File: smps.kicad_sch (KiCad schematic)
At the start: 36 parts, among them J1 Screw_Terminal_01x02, J4 Screw_Terminal_01x02, U1 LT8640S

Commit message: Cosmetic updates
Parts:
- H1, H2, H3, H4: footprint MountingHole:MountingHole_3.2mm_M3_Pad -> MountingHole:MountingHole_3.2mm_M3
- renumbered TP2 to TP1, TP1 to TP2
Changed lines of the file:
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@@
       (effects (font (size 1.27 1.27)) (justify left))
     )
-    (property "Footprint" "MountingHole:MountingHole_3.2mm_M3_Pad" (id 2) (at 16.51 182.88 0)
+    (property "Footprint" "MountingHole:MountingHole_3.2mm_M3" (id 2) (at 16.51 182.88 0)
       (effects (font (size 1.27 1.27)) hide)
     )
@@
       (effects (font (size 1.27 1.27)) (justify left))
     )
-    (property "Footprint" "MountingHole:MountingHole_3.2mm_M3_Pad" (id 2) (at 16.51 187.96 0)
+    (property "Footprint" "MountingHole:MountingHole_3.2mm_M3" (id 2) (at 16.51 187.96 0)
       (effects (font (size 1.27 1.27)) hide)
     )
@@
   (symbol (lib_id "Connector:TestPoint") (at 142.24 109.22 270) (unit 1)
     (in_bom yes) (on_board yes)
-    (property "Reference" "TP2" (id 0) (at 143.51 111.76 90)
+    (property "Reference" "TP1" (id 0) (at 140.97 111.76 90)
       (effects (font (size 1.27 1.27)) (justify left))
     )
@@
   (symbol (lib_id "Connector:TestPoint") (at 142.24 119.38 270) (unit 1)
     (in_bom yes) (on_board yes)
-    (property "Reference" "TP1" (id 0) (at 143.51 121.92 90)
+    (property "Reference" "TP2" (id 0) (at 140.97 121.92 90)
       (effects (font (size 1.27 1.27)) (justify left))
     )
@@
       (effects (font (size 1.27 1.27)) (justify left))
     )
-    (property "Footprint" "MountingHole:MountingHole_3.2mm_M3_Pad" (id 2) (at 16.51 177.8 0)
+    (property "Footprint" "MountingHole:MountingHole_3.2mm_M3" (id 2) (at 16.51 177.8 0)
       (effects (font (size 1.27 1.27)) hide)
     )
@@
       (effects (font (size 1.27 1.27)) (justify left))
     )
-    (property "Footprint" "MountingHole:MountingHole_3.2mm_M3_Pad" (id 2) (at 16.51 193.04 0)
+    (property "Footprint" "MountingHole:MountingHole_3.2mm_M3" (id 2) (at 16.51 193.04 0)
       (effects (font (size 1.27 1.27)) hide)
     )
@@
     )
     (path "/be315ce4-7106-45b7-89c2-89dbb67c559b"
-      (reference "H1") (unit 1) (value "MountingHole") (footprint "MountingHole:MountingHole_3.2mm_M3_Pad")
+      (reference "H1") (unit 1) (value "MountingHole") (footprint "MountingHole:MountingHole_3.2mm_M3")
     )
     (path "/2551a458-2f16-43a1-81b9-4f1543bf4a19"
-      (reference "H2") (unit 1) (value "MountingHole") (footprint "MountingHole:MountingHole_3.2mm_M3_Pad")
+      (reference "H2") (unit 1) (value "MountingHole") (footprint "MountingHole:MountingHole_3.2mm_M3")
     )
     (path "/52837943-e32c-4fde-ad45-22a60a17bb4c"
-      (reference "H3") (unit 1) (value "MountingHole") (footprint "MountingHole:MountingHole_3.2mm_M3_Pad")
+      (reference "H3") (unit 1) (value "MountingHole") (footprint "MountingHole:MountingHole_3.2mm_M3")
     )
     (path "/f8c5f4b7-2afc-41c5-bf7d-f4b92a6455d0"
-      (reference "H4") (unit 1) (value "MountingHole") (footprint "MountingHole:MountingHole_3.2mm_M3_Pad")
+      (reference "H4") (unit 1) (value "MountingHole") (footprint "MountingHole:MountingHole_3.2mm_M3")
     )
     (path "/aa8d5637-fa2c-4b11-aa5d-afb55fed7b9f"
@@
       (reference "R5") (unit 1) (value "2.2k") (footprint "Resistor_SMD:R_0805_2012Metric")
     )
+    (path "/b19cdc07-4c16-4749-8880-5b1b66233ab4"
+      (reference "TP1") (unit 1) (value "TestPoint") (footprint "TestPoint:TestPoint_Pad_D1.0mm")
+    )
     (path "/b5bac656-fbb4-4047-8c0d-8404ecf39e3d"
-      (reference "TP1") (unit 1) (value "TestPoint") (footprint "TestPoint:TestPoint_Pad_D1.0mm")
-    )
-    (path "/b19cdc07-4c16-4749-8880-5b1b66233ab4"
       (reference "TP2") (unit 1) (value "TestPoint") (footprint "TestPoint:TestPoint_Pad_D1.0mm")
     )

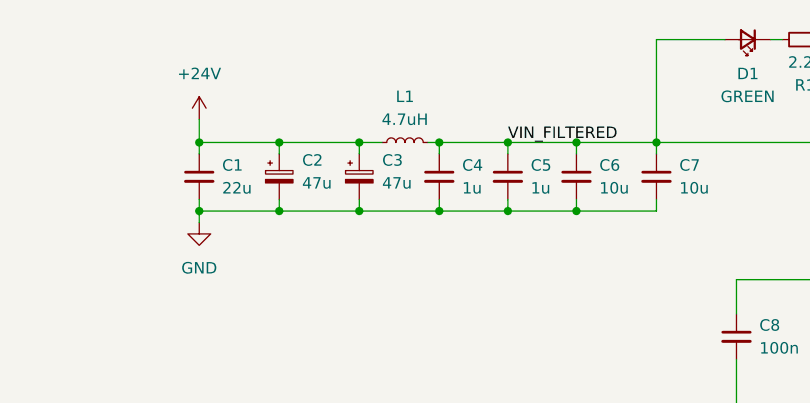
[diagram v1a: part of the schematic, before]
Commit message: Fix L1 input coil value
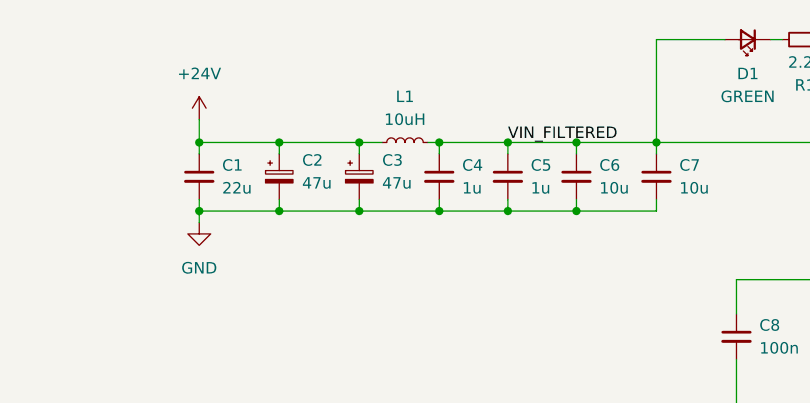
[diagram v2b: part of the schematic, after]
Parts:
- L1: value 4.7uH -> 10uH
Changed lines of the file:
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@@
     (in_bom yes) (on_board yes) (fields_autoplaced)
     (property "Reference" "L1" (id 0) (at 62.23 73.66 90))
-    (property "Value" "4.7uH" (id 1) (at 62.23 76.2 90))
+    (property "Value" "10uH" (id 1) (at 62.23 76.2 90))
     (property "Footprint" "Inductor_SMD:L_Wuerth_WE-PD-Typ-LS_Handsoldering" (id 2) (at 62.23 78.74 0)
       (effects (font (size 1.27 1.27)) hide)
@@
     )
     (path "/972cc210-f8c2-4b7b-91fa-7eea1f2e42c7"
-      (reference "L1") (unit 1) (value "4.7uH") (footprint "Inductor_SMD:L_Wuerth_WE-PD-Typ-LS_Handsoldering")
+      (reference "L1") (unit 1) (value "10uH") (footprint "Inductor_SMD:L_Wuerth_WE-PD-Typ-LS_Handsoldering")
     )
     (path "/b638c7df-3e06-4f0a-938c-acf46b5528f1"
